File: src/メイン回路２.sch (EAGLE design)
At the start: 24 parts

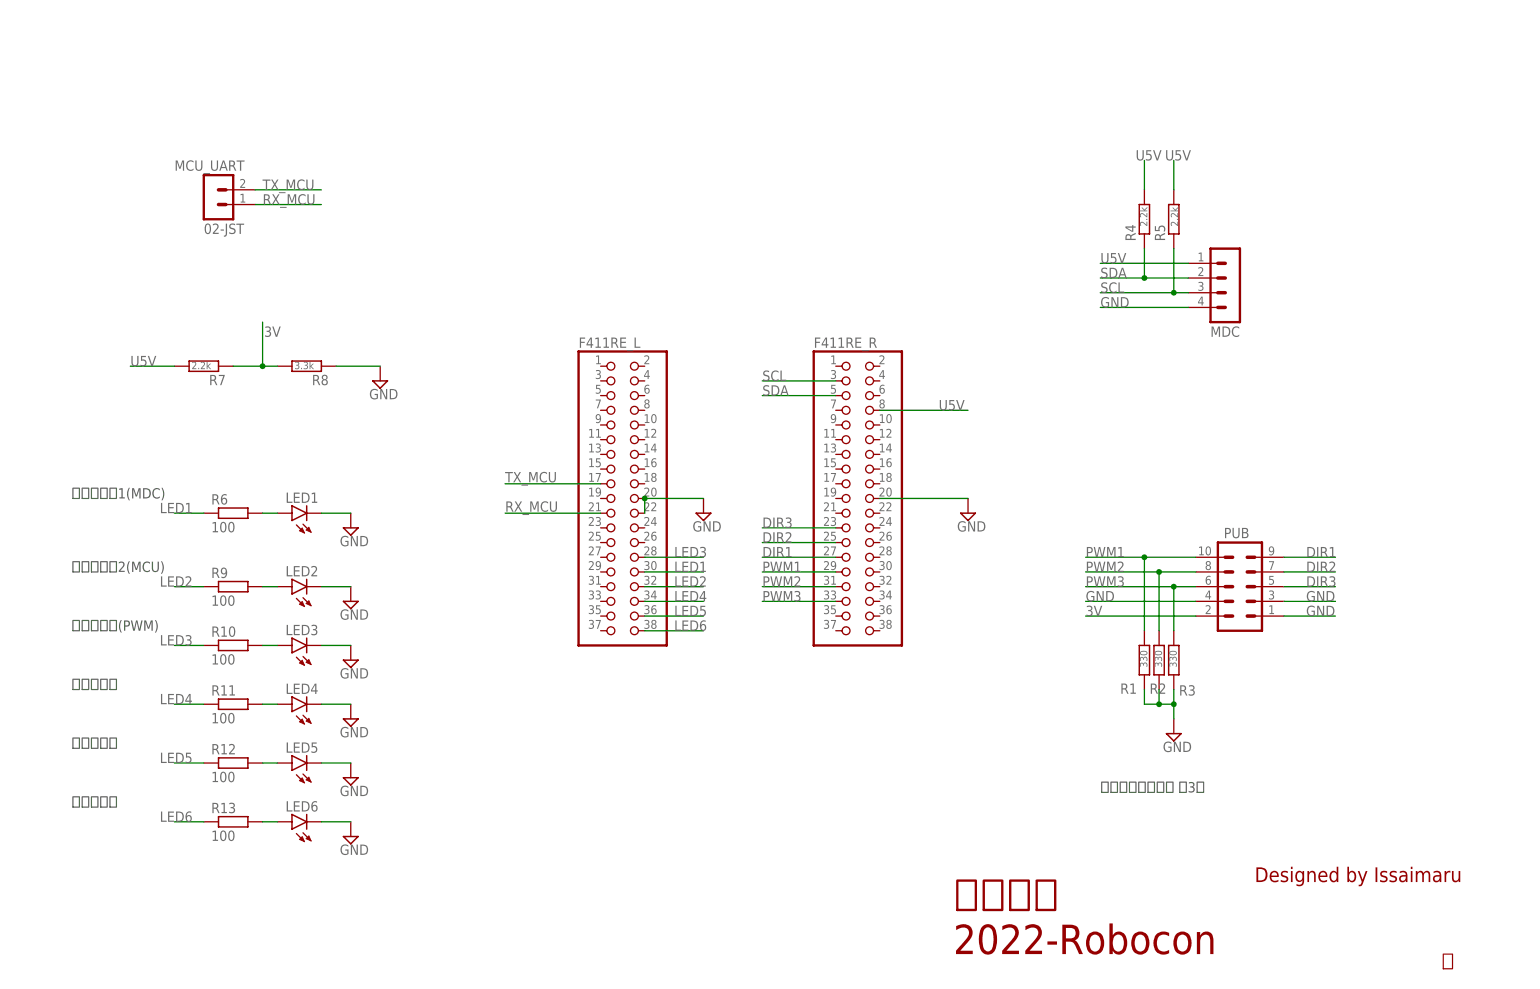
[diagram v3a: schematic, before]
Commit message: [fix]メイン回路2.schの修正
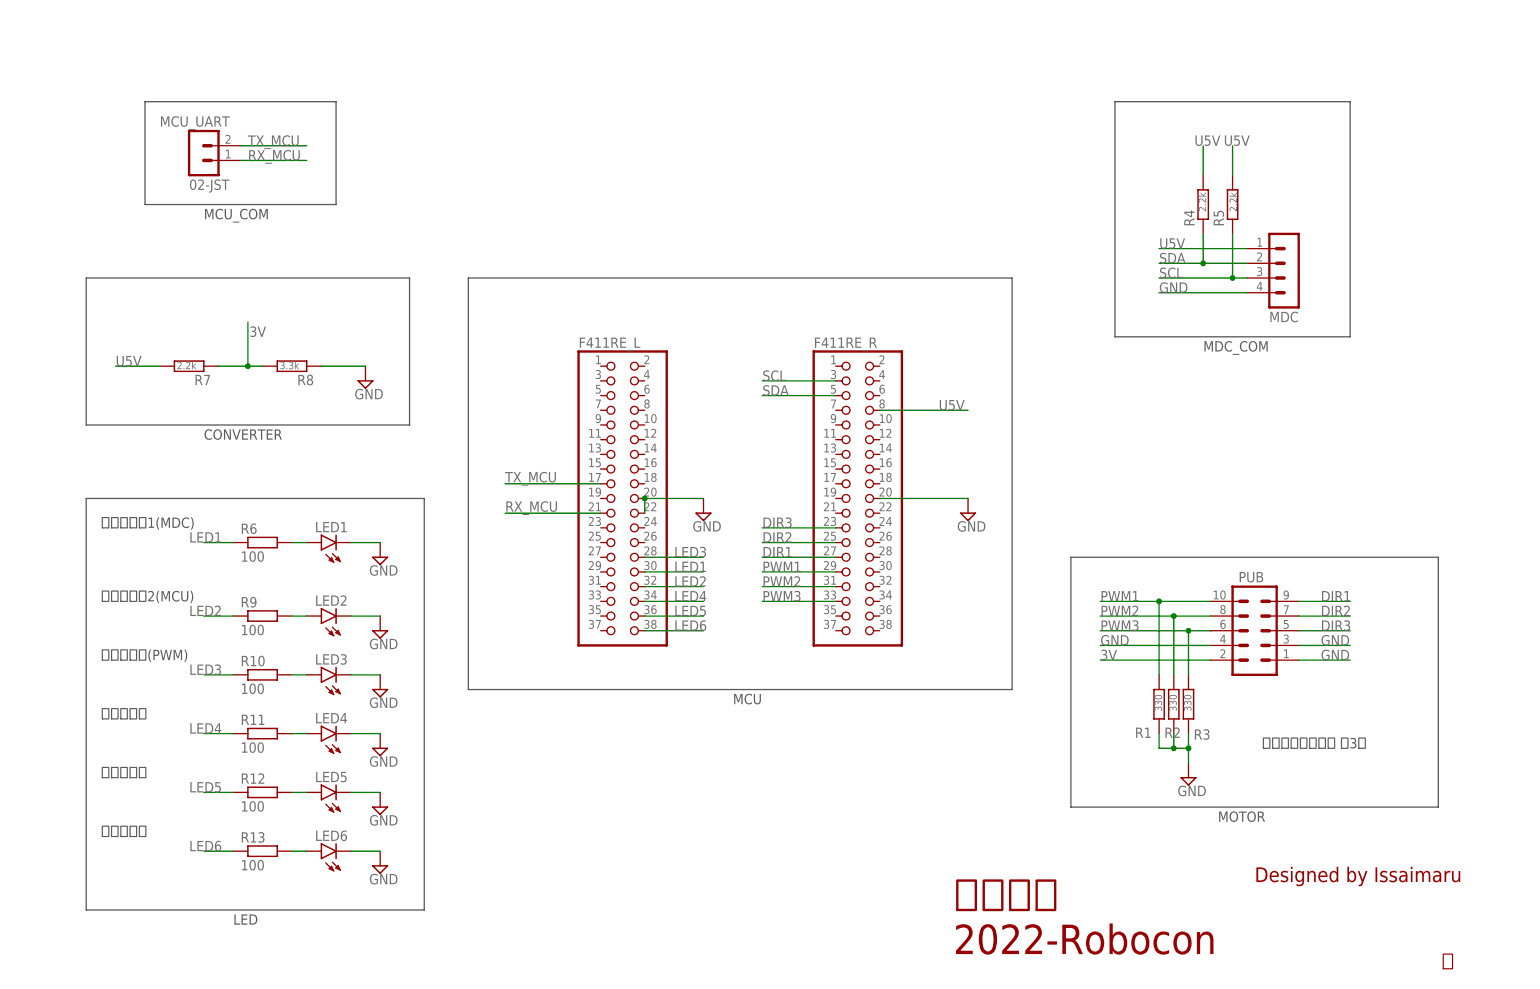
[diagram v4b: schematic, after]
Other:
- note added: "CONVERTER"
- note added: "LED"
- note added: "MCU"
- note added: "MCU_COM"
- note added: "MDC_COM"
- note added: "MOTOR"
- moved on the sheet: LED1, LED2, LED3, LED4, LED5, LED6, MCU_UART, MDC, PUB, R1, R10, R11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

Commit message: [complete]メイン回路1の完成
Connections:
- net DIR1: now also F411RE_R.29; no longer F411RE_R.27
- net DIR2: now also F411RE_R.31; no longer F411RE_R.25
- net DIR3: now also F411RE_R.33; no longer F411RE_R.23
- net PWM1: now also F411RE_R.27; no longer F411RE_R.29
- net PWM2: now also F411RE_R.25; no longer F411RE_R.31
- net PWM3: now also F411RE_R.23; no longer F411RE_R.33
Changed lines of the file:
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@@
 </segment>
 <segment>
-<pinref part="F411RE_R" gate="G$1" pin="31"/>
-<wire x1="144.78" y1="71.12" x2="132.08" y2="71.12" width="0.1524" layer="91"/>
-<label x="132.08" y="71.12" size="1.778" layer="95"/>
+<pinref part="F411RE_R" gate="G$1" pin="25"/>
+<wire x1="144.78" y1="78.74" x2="132.08" y2="78.74" width="0.1524" layer="91"/>
+<label x="132.08" y="78.74" size="1.778" layer="95"/>
 </segment>
 </net>
@@
 </segment>
 <segment>
-<pinref part="F411RE_R" gate="G$1" pin="33"/>
-<wire x1="144.78" y1="68.58" x2="132.08" y2="68.58" width="0.1524" layer="91"/>
-<label x="132.08" y="68.58" size="1.778" layer="95"/>
+<pinref part="F411RE_R" gate="G$1" pin="23"/>
+<wire x1="144.78" y1="81.28" x2="132.08" y2="81.28" width="0.1524" layer="91"/>
+<label x="132.08" y="81.28" size="1.778" layer="95"/>
 </segment>
 </net>
@@
 </segment>
 <segment>
-<pinref part="F411RE_R" gate="G$1" pin="27"/>
-<wire x1="144.78" y1="76.2" x2="132.08" y2="76.2" width="0.1524" layer="91"/>
-<label x="132.08" y="76.2" size="1.778" layer="95"/>
+<pinref part="F411RE_R" gate="G$1" pin="29"/>
+<wire x1="144.78" y1="73.66" x2="132.08" y2="73.66" width="0.1524" layer="91"/>
+<label x="132.08" y="73.66" size="1.778" layer="95"/>
 </segment>
 </net>
@@
 </segment>
 <segment>
-<pinref part="F411RE_R" gate="G$1" pin="25"/>
-<wire x1="144.78" y1="78.74" x2="132.08" y2="78.74" width="0.1524" layer="91"/>
-<label x="132.08" y="78.74" size="1.778" layer="95"/>
+<pinref part="F411RE_R" gate="G$1" pin="31"/>
+<wire x1="144.78" y1="71.12" x2="132.08" y2="71.12" width="0.1524" layer="91"/>
+<label x="132.08" y="71.12" size="1.778" layer="95"/>
 </segment>
 </net>
@@
 </segment>
 <segment>
-<pinref part="F411RE_R" gate="G$1" pin="23"/>
-<wire x1="144.78" y1="81.28" x2="132.08" y2="81.28" width="0.1524" layer="91"/>
-<label x="132.08" y="81.28" size="1.778" layer="95"/>
+<pinref part="F411RE_R" gate="G$1" pin="33"/>
+<wire x1="144.78" y1="68.58" x2="132.08" y2="68.58" width="0.1524" layer="91"/>
+<label x="132.08" y="68.58" size="1.778" layer="95"/>
 </segment>
 </net>
@@
 </segment>
 <segment>
-<pinref part="F411RE_R" gate="G$1" pin="29"/>
-<wire x1="144.78" y1="73.66" x2="132.08" y2="73.66" width="0.1524" layer="91"/>
-<label x="132.08" y="73.66" size="1.778" layer="95"/>
+<pinref part="F411RE_R" gate="G$1" pin="27"/>
+<wire x1="144.78" y1="76.2" x2="132.08" y2="76.2" width="0.1524" layer="91"/>
+<label x="132.08" y="76.2" size="1.778" layer="95"/>
 </segment>
 </net>

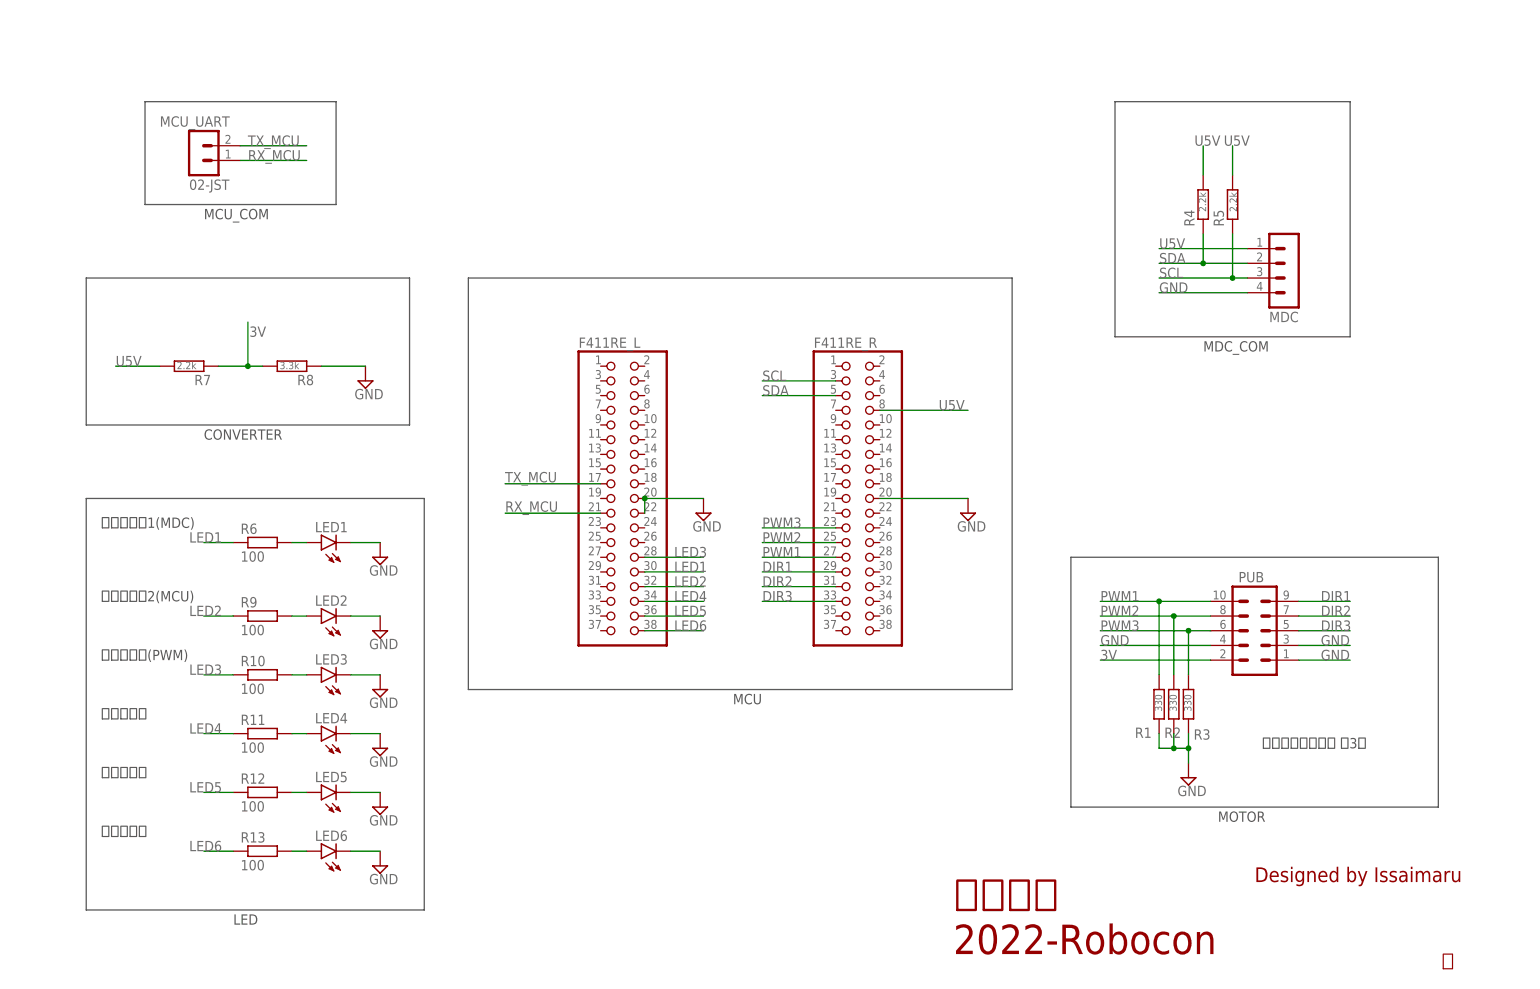
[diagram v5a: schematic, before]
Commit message: [complete]メイン回路2に暴走対策回路を追加
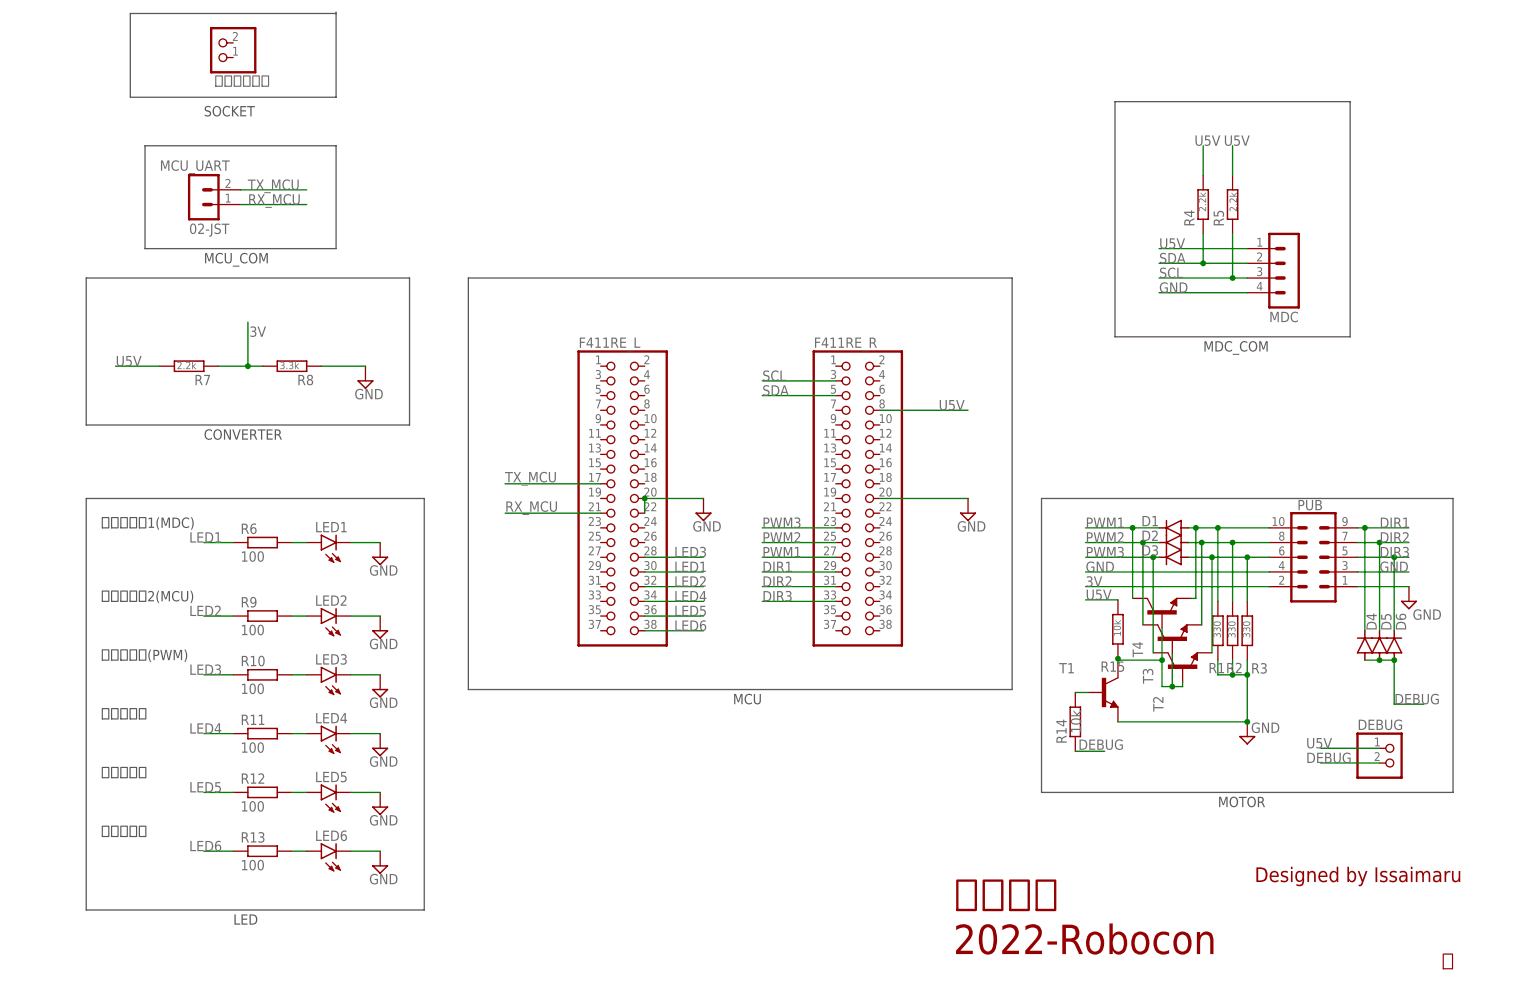
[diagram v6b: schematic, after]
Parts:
- added D1, D2, D3, D4, D5, D6: 1N4004, diode:1N4004
- added DEBUG, ソケット置き: (no value), pinhead:PINHD-1X2
- added R14, R15: 10k, rcl:R-EU_0204/7
- added T1, T2, T3, T4: 一般的なトランジスタ, 一般的なトランジスタ:一般的なトランジスタ
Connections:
- new net DEBUG: D4.A, D5.A, D6.A, DEBUG.2, R14.1
- new net N$7: R14.2, T1.B
- new net N$8: D1.A, PUB.10, R1.2, T4.E
- new net N$9: D2.A, PUB.8, R2.2, T3.E
- new net N$Q0: D3.A, PUB.6, R3.2, T2.E
- new net ZM: R15.1, T1.C, T2.B, T3.B, T4.B
- net DIR1: now also D4.C
- net DIR2: now also D5.C
- net DIR3: now also D6.C
- net GND: now also T1.E
- net PWM1: now also D1.C, T4.C; no longer PUB.10, R1.2
- net PWM2: now also D2.C, T3.C; no longer PUB.8, R2.2
- net PWM3: now also D3.C, T2.C; no longer PUB.6, R3.2
- net U5V: now also DEBUG.1, R15.2
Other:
- note added: "SOCKET"
- note removed: "上下，装填，射出 計3つ"
- moved on the sheet: MCU_UART, PUB, R1, R2, R3
